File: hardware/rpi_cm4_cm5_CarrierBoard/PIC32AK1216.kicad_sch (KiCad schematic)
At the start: 84 parts, among them J10 PR20206VBNN, U1 PIC32AK1216GC41064-I/M7, Y3 20MHz

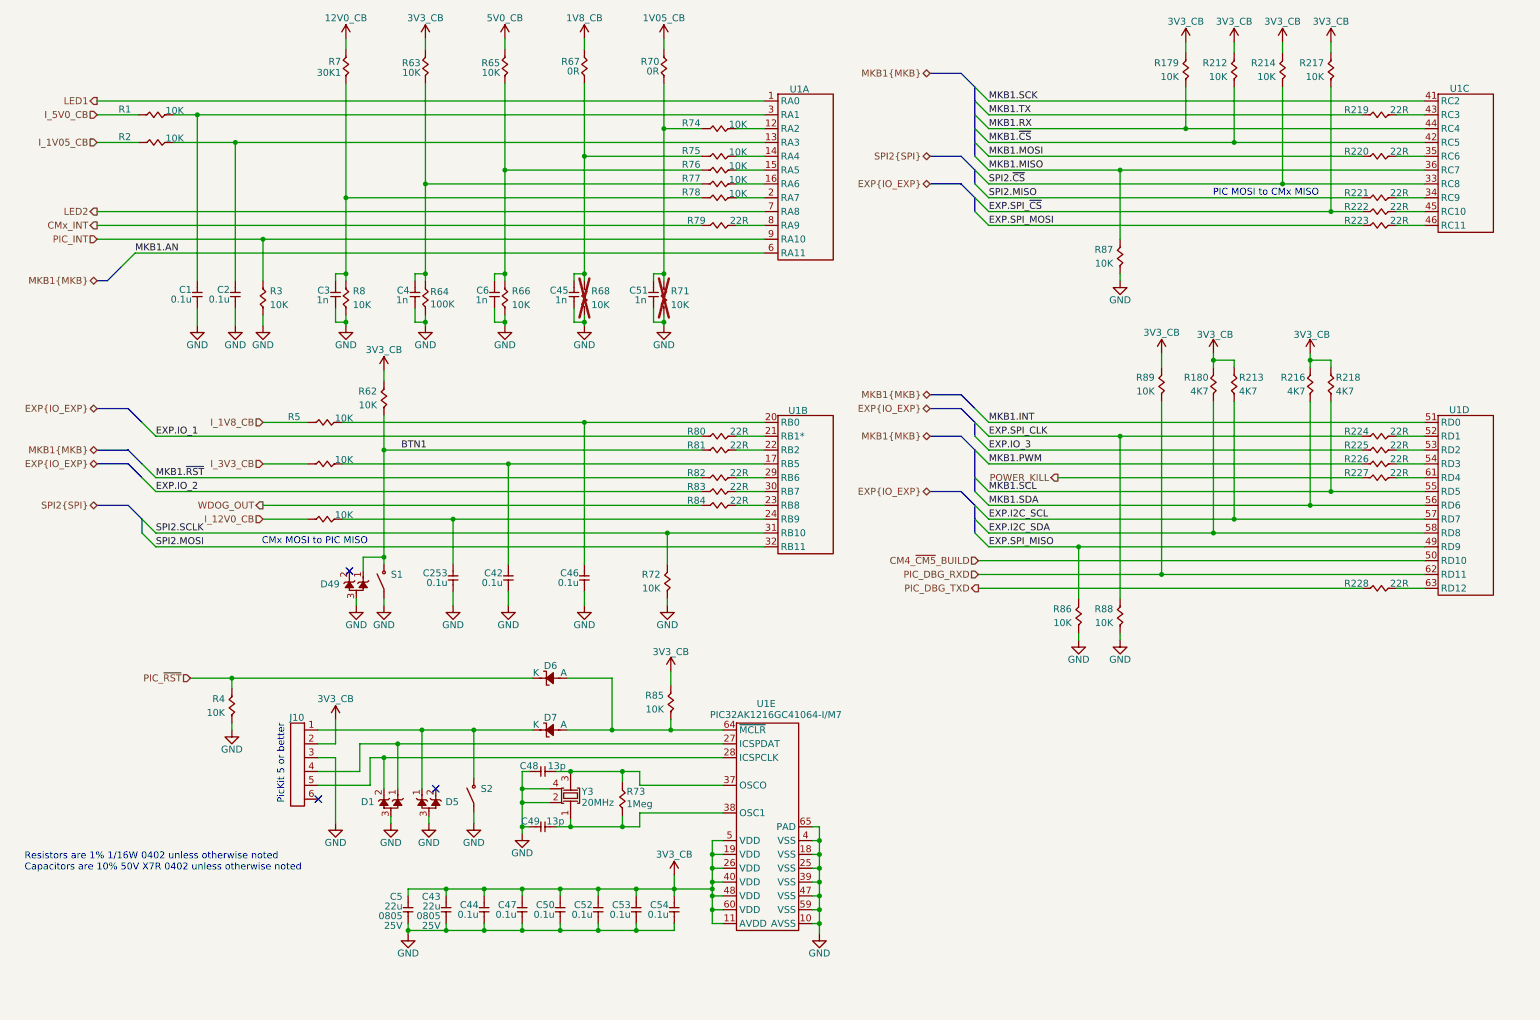
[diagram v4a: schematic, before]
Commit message: Finished implementation of watchdog circuit All possible reset scenarios documented
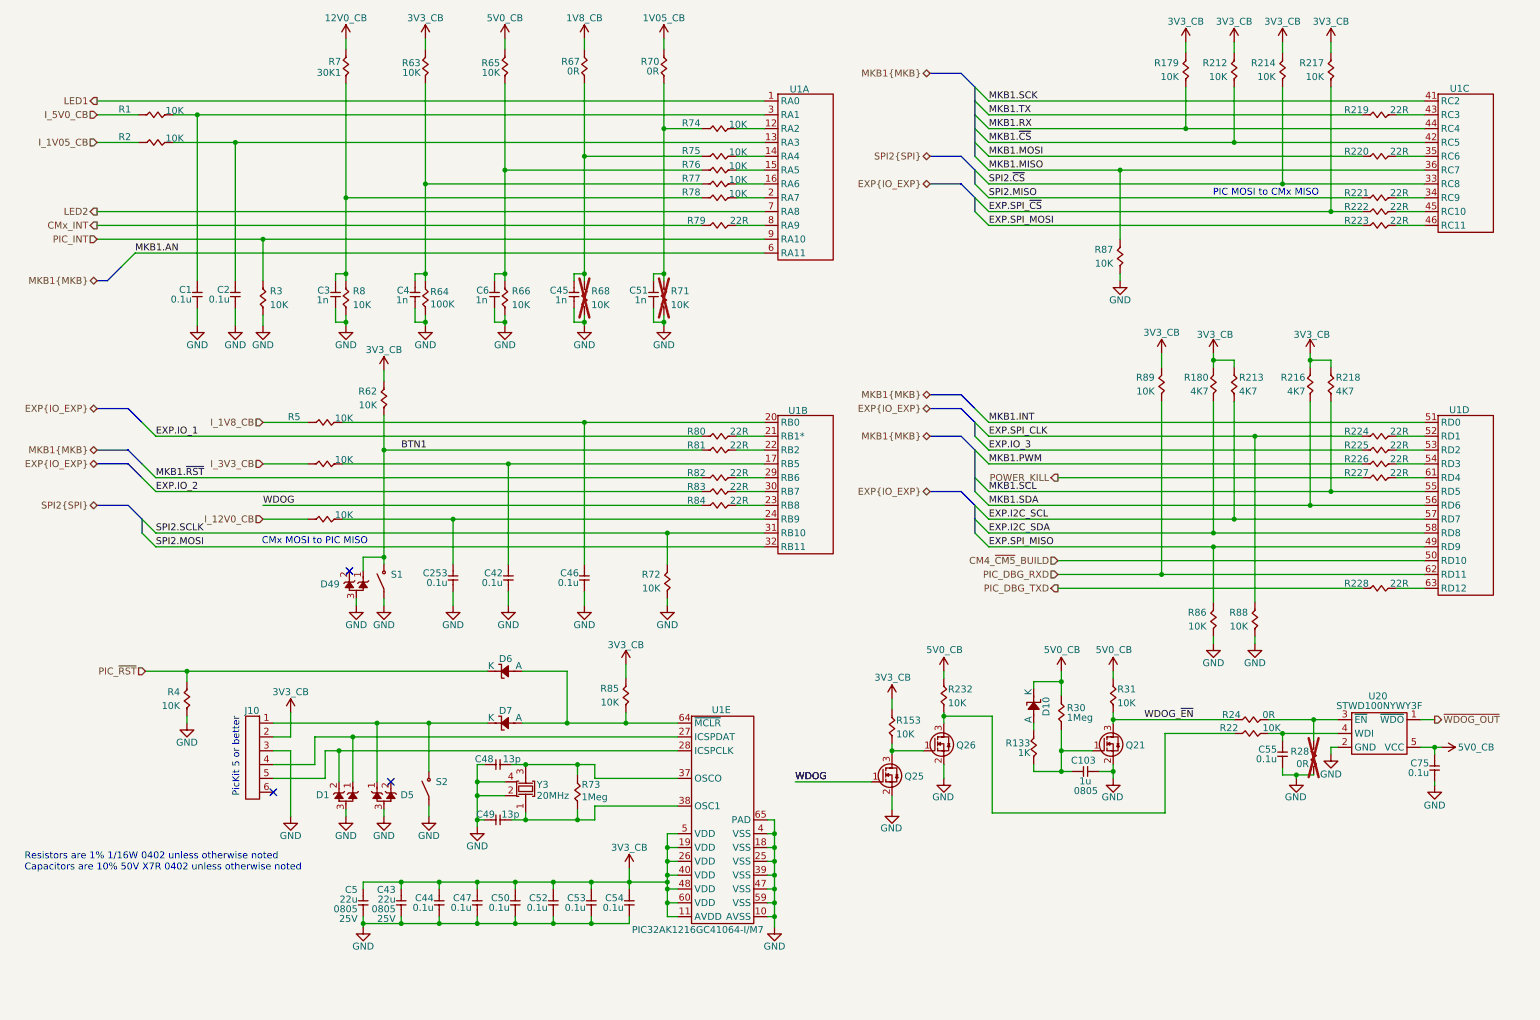
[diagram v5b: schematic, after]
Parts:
- added C103: 1u, footprint:CAP_NONPOL_0805, symbol KicadCompDb:Capacitors/CAP_CER_SMT_00002
- added C55, C75: 0.1u, footprint:CAP_NONPOL_0402, symbol KicadCompDb:Capacitors/CAP_CER_SMT_00001
- added D10: BAT42WS-TP, footprint:SOD-323, symbol KicadCompDb:Diodes/DIODE_00006
- added Q21, Q25, Q26: 2N7002, footprint:SOT-23-3, symbol KicadCompDb:Mosfet/MOSFET_00001
- added R133: 1K, footprint:RES_0402, symbol KicadCompDb:Resistors/RES_SMT_00004
- added R153, R22, R232, R31: 10K, footprint:RES_0402, symbol KicadCompDb:Resistors/RES_SMT_00013
- added R24, R28: 0R, footprint:RES_0402, symbol KicadCompDb:Resistors/RES_SMT_00001
- added R30: 1Meg, footprint:RES_0402, symbol KicadCompDb:Resistors/RES_SMT_00006
- added U20: STWD100NYWY3F, footprint:SOT-23-5, symbol KicadCompDb:Logic/LOGIC_00007
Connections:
- net 3V3_CB: now also R153.2
- net 5V0_CB: now also C75.2, D10.1 (K), R232.2, R30.2, R31.2, U20.5 (VCC)
- net GND: now also C103.1, C55.1, C75.1, Q21.2 (S), Q25.2 (S), Q26.2 (S), R28.1, U20.2 (GND)
- net WDOG_OUT renamed WDOG
- net WDOG: now also Q25.1 (G)
- new net: Q25.3 (D), Q26.1 (G), R153.1
- new net: Q26.3 (D), R22.2, R232.1
- new net: C103.2, Q21.1 (G), R133.1, R30.1
- new net: R24.1, R28.2, U20.3 (~{EN})
- new net: D10.2 (A), R133.2
- new net: C55.2, R22.1, U20.4 (WDI)
- new net WDOG_~{EN}: Q21.3 (D), R24.2, R31.1
- new net ~{WDOG_OUT}: U20.1 (~{WDO})
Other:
- moved on the sheet: C43, C44, C47, C48, C49, C5, C50, C52, C53, C54, D1, D5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

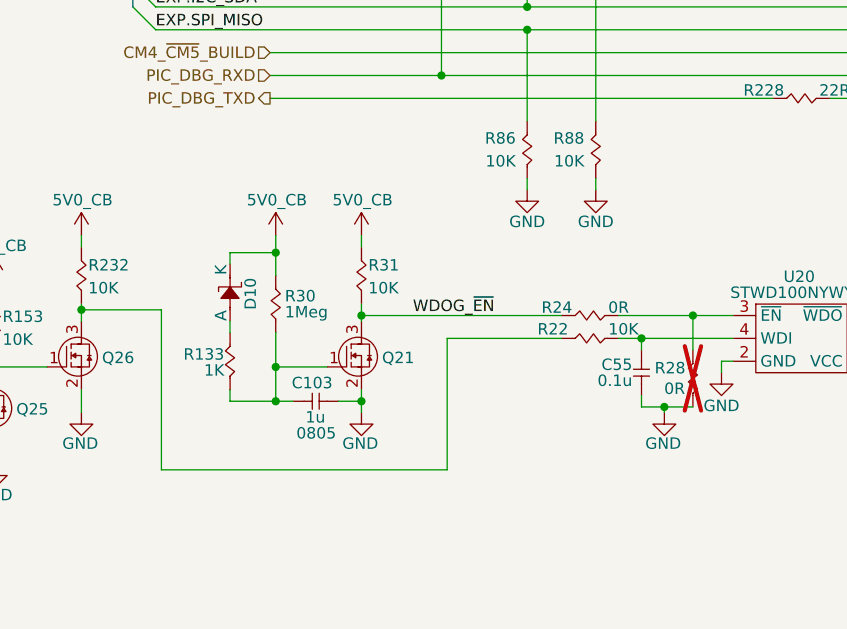
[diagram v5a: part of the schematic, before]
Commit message: Update preliminary placement, update DNP, regen BOM + Preliminary schematics
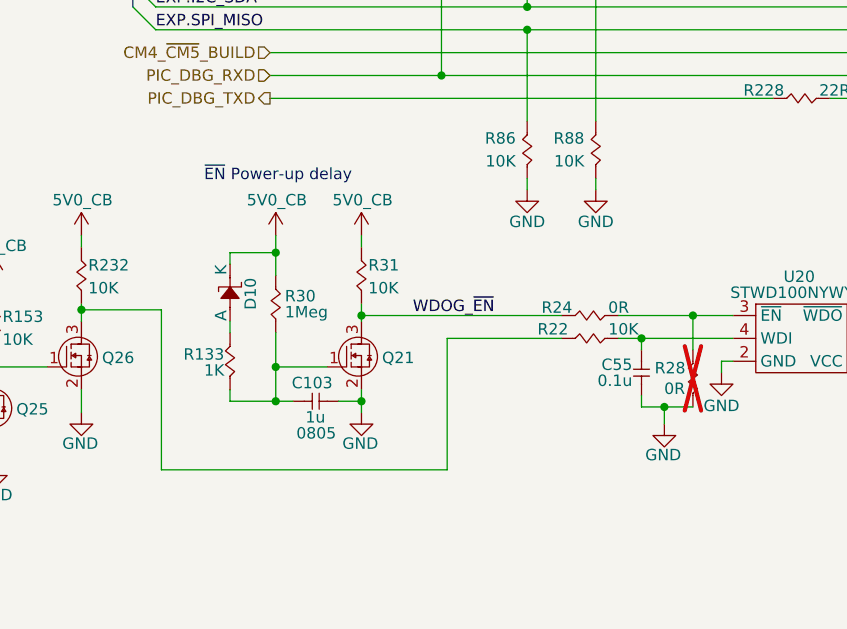
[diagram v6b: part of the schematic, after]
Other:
- note added: "~{EN} Power-up delay"
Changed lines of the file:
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@@
 		)
 	)
+	(text "~{EN} Power-up delay"
+		(exclude_from_sim no)
+		(at 203.454 129.286 0)
+		(effects
+			(font
+				(size 1.27 1.27)
+				(color 255 153 0 1)
+			)
+		)
+	)
 	(junction
 		(at 114.3 153.035)
@@
 	(wire
 		(pts
-			(xy 246.38 154.94) (xy 246.38 155.575)
+			(xy 246.38 154.94) (xy 246.38 156.845)
 		)
 		(stroke
@@
 	(symbol
 		(lib_id "KiCad_Pwr_Symbols:GND")
-		(at 246.38 155.575 0)
+		(at 246.38 156.845 0)
 		(unit 1)
 		(exclude_from_sim no)
@@
 		(dnp no)
 		(property "Reference" "#PWR088"
-			(at 246.38 161.925 0)
+			(at 246.38 163.195 0)
 			(effects
 				(font
@@
 		)
 		(property "Value" "GND"
-			(at 246.253 159.004 0)
+			(at 246.253 160.274 0)
 			(effects
 				(font
@@
 		)
 		(property "Footprint" ""
-			(at 246.38 155.575 0)
+			(at 246.38 156.845 0)
 			(effects
 				(font
@@
 		)
 		(property "Datasheet" ""
-			(at 246.38 155.575 0)
+			(at 246.38 156.845 0)
 			(effects
 				(font
@@
 		)
 		(property "Description" "Power symbol creates a global label with name \"GND\" , ground"
-			(at 246.38 155.575 0)
+			(at 246.38 156.845 0)
 			(effects
 				(font

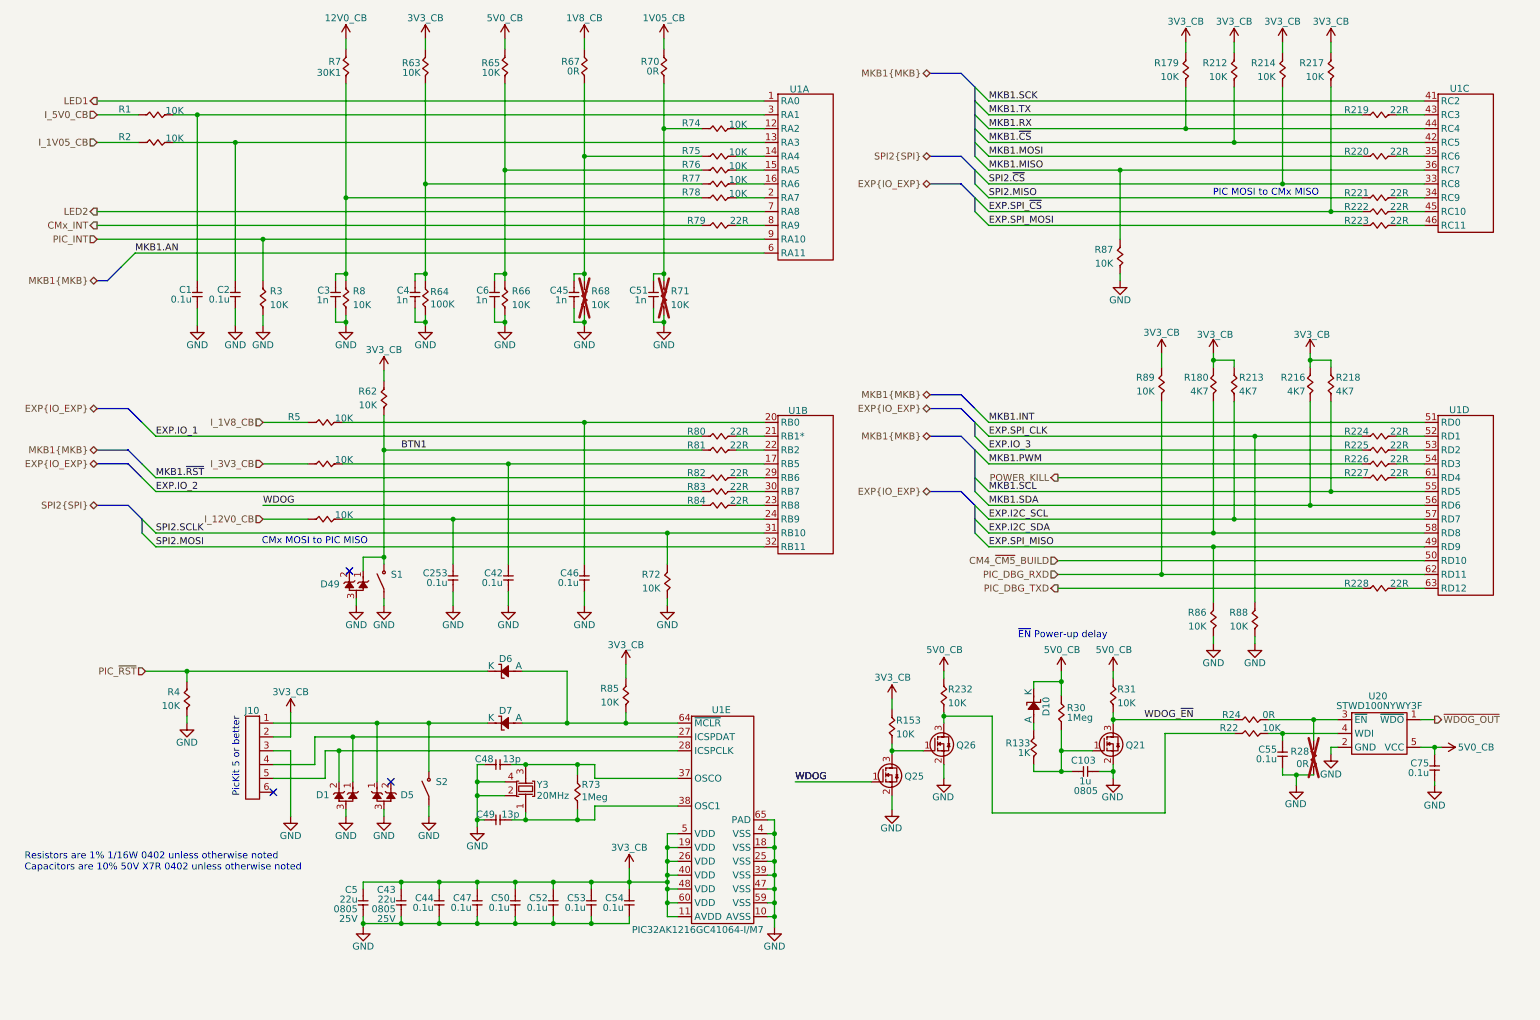
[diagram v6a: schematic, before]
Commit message: Update PCB design rules for outer layers differential pairs Update preliminary component placement Update schematics based on PCB placement & remove duplicata / unnecessary components Update design notes and power table
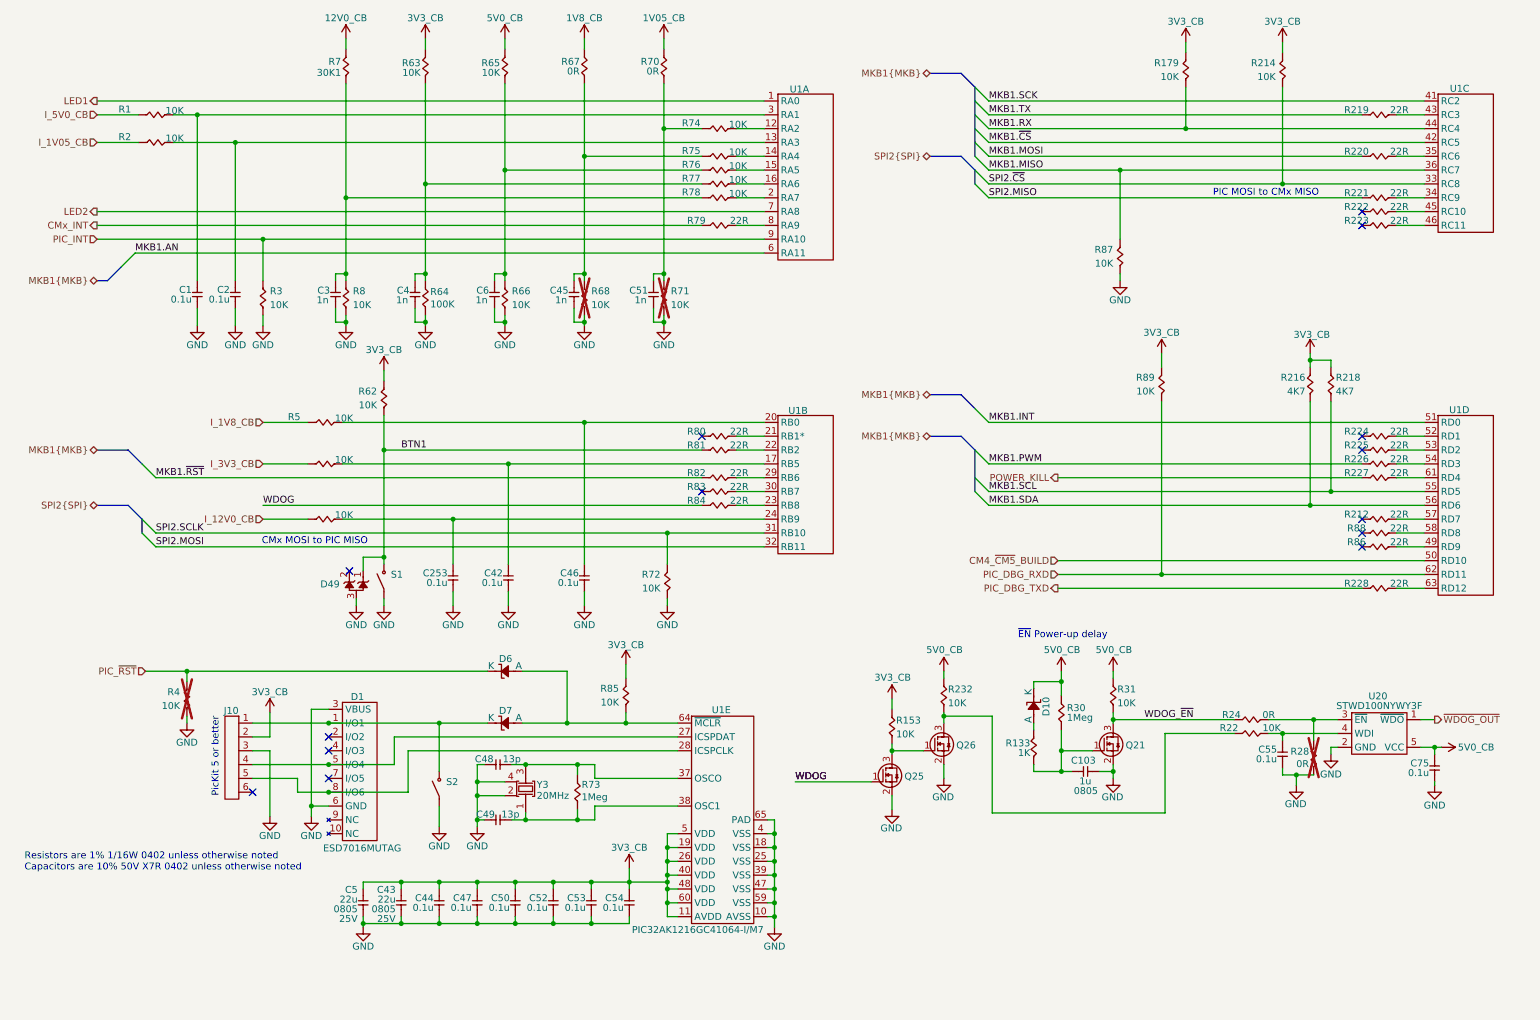
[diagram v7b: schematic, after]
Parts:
- removed D1, D5: D1213A-02SOL-7, footprint:SOT-23-3, symbol KicadCompDb:ESD Diodes/ESD_DIODE_00002
- removed R180, R213: 4K7, footprint:RES_0402, symbol KicadCompDb:Resistors/RES_SMT_00010
- removed R212, R217, R86, R88: 10K, footprint:RES_0402, symbol KicadCompDb:Resistors/RES_SMT_00013
- added D1: ESD7016MUTAG, footprint:UDFN8, symbol KicadCompDb:ESD Diodes/ESD_DIODE_00001
- added R212, R86, R88: 22R, footprint:RES_0402, symbol KicadCompDb:Resistors/RES_SMT_00015
- R4: now not fitted
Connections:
- net GND: now also D1.3 (VBUS), D1.6 (GND)
- net at J10.4, U1.27 (ICSPDAT): now also D1.5 (I/O4)
- net at J10.5, U1.28 (ICSPCLK): now also D1.8 (I/O6)
- net at D7.1 (K), J10.1, S2.2: now also D1.1 (I/O1)
- net EXP.I2C_SCL: no longer names the net of U1.57 (RD7)
- net EXP.I2C_SCL: now also R212.1
- net EXP.I2C_SDA: no longer names the net of U1.58 (RD8)
- net EXP.I2C_SDA: now also R88.1
- net EXP.IO_1: no longer names the net of R80.2
- net EXP.IO_2: no longer names the net of R83.2
- net EXP.IO_3: no longer names the net of R225.2
- net EXP.SPI_CLK: no longer names the net of R224.2
- net EXP.SPI_MISO: no longer names the net of U1.49 (RD9)
- net EXP.SPI_MISO: now also R86.1
- net EXP.SPI_MOSI: no longer names the net of R223.2
- net EXP.SPI_~{CS}: no longer names the net of R222.2
- no-connect marks 3 -> 14
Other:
- moved on the sheet: J10, S2
